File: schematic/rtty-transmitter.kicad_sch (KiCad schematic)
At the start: 67 parts, among them J1 USB_B, J2 USBasp header, J3 Conn_Coaxial, J4 Conn_01x02_Pin, J5 Conn_01x02_Pin, J6 Conn_01x02_Pin, Q1 PN2222A, Q2 PN2222A, U1 MCP2221AxP, U2 ATmega328P-P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

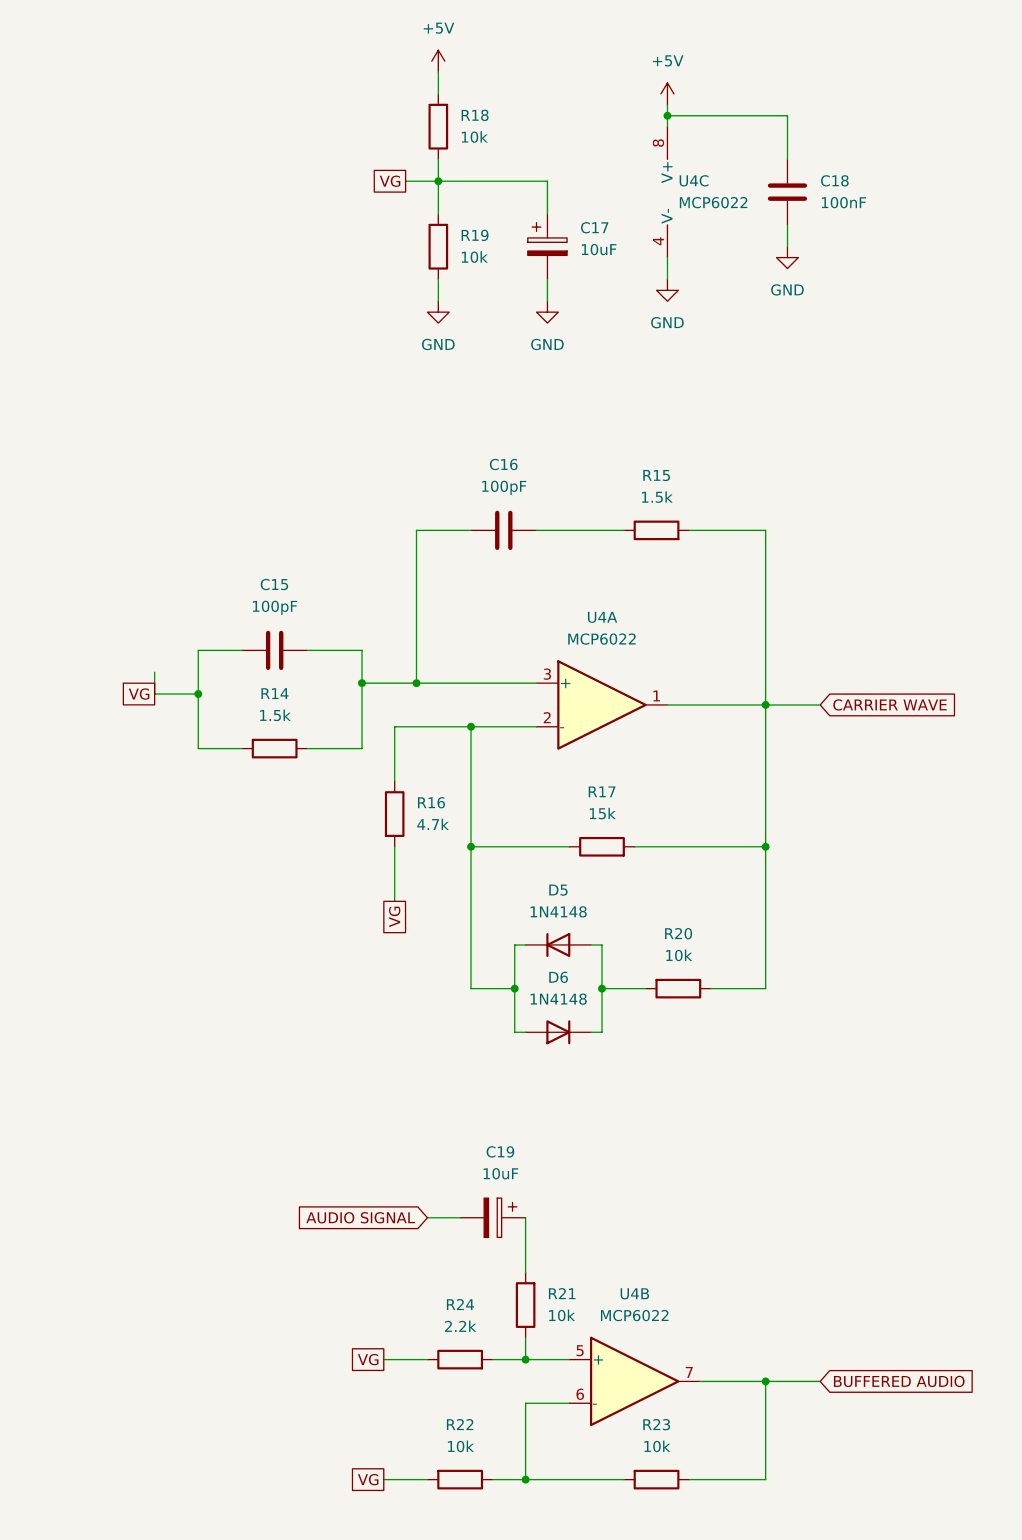
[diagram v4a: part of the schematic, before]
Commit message: Schematic: Test points added
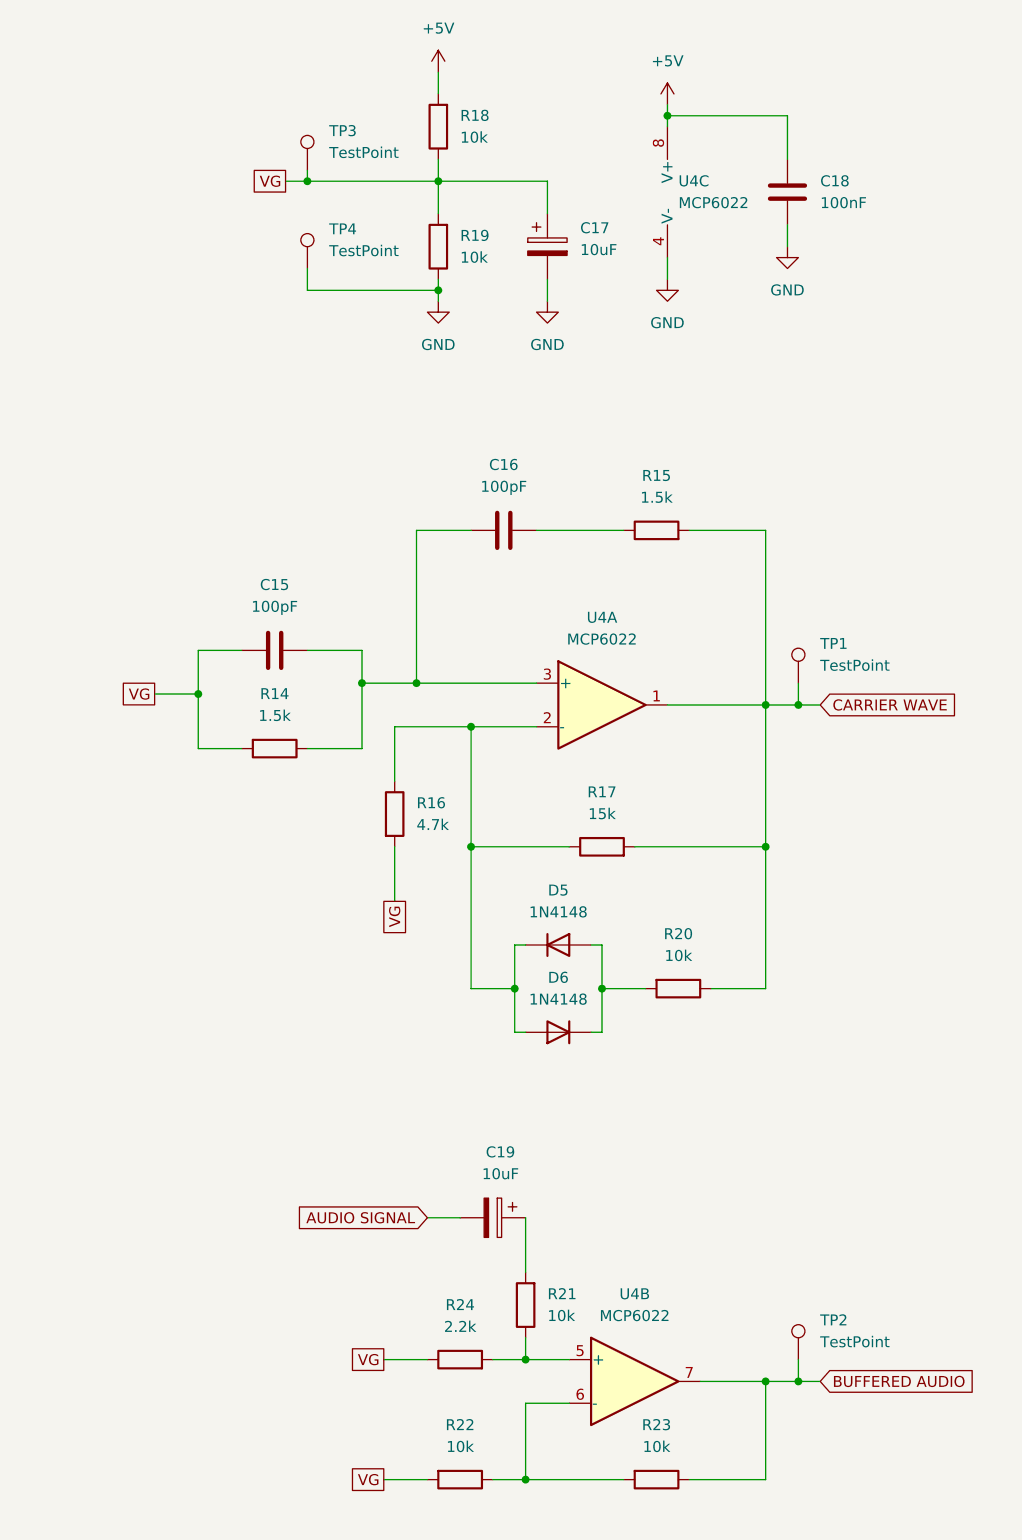
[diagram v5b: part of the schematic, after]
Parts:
- added TP1, TP2, TP3, TP4: TestPoint, TestPoint:TestPoint_Plated_Hole_D2.0mm, symbol Connector:TestPoint
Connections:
- net BUFFERED AUDIO: now also TP2.1
- net CARRIER WAVE: now also TP1.1
- net GND: now also TP4.1
- net VG: now also TP3.1
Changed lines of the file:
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@@
   (junction (at 194.31 124.46) (diameter 0) (color 0 0 0 0)
   )
+  (junction (at 335.28 55.88) (diameter 0) (color 0 0 0 0)
+  )
   (junction (at 180.34 81.28) (diameter 0) (color 0 0 0 0)
   )
   (junction (at 200.66 252.73) (diameter 0) (color 0 0 0 0)
   )
+  (junction (at 377.19 182.88) (diameter 0) (color 0 0 0 0)
+  )
   (junction (at 53.34 185.42) (diameter 0) (color 0 0 0 0)
   )
@@
   (junction (at 248.92 54.61) (diameter 0) (color 0 0 0 0)
   )
+  (junction (at 320.04 43.18) (diameter 0) (color 0 0 0 0)
+  )
   (junction (at 92.71 127) (diameter 0) (color 0 0 0 0)
   )
@@
   (junction (at 339.09 106.68) (diameter 0) (color 0 0 0 0)
   )
+  (junction (at 377.19 104.14) (diameter 0) (color 0 0 0 0)
+  )
   (junction (at 335.28 43.18) (diameter 0) (color 0 0 0 0)
   )
@@
     (stroke (width 0) (type default))
   )
-  (wire (pts (xy 373.38 104.14) (xy 379.73 104.14))
+  (wire (pts (xy 373.38 104.14) (xy 377.19 104.14))
     (stroke (width 0) (type default))
   )
@@
     (stroke (width 0) (type default))
   )
+  (wire (pts (xy 320.04 55.88) (xy 335.28 55.88))
+    (stroke (width 0) (type default))
+  )
   (wire (pts (xy 200.66 241.3) (xy 200.66 243.84))
     (stroke (width 0) (type default))
@@
     (stroke (width 0) (type default))
   )
+  (wire (pts (xy 320.04 53.34) (xy 320.04 55.88))
+    (stroke (width 0) (type default))
+  )
   (wire (pts (xy 246.38 87.63) (xy 226.06 87.63))
     (stroke (width 0) (type default))
@@
     (stroke (width 0) (type default))
   )
+  (wire (pts (xy 377.19 101.6) (xy 377.19 104.14))
+    (stroke (width 0) (type default))
+  )
   (wire (pts (xy 67.31 66.04) (xy 67.31 58.42))
     (stroke (width 0) (type default))
@@
     (stroke (width 0) (type default))
   )
+  (wire (pts (xy 377.19 182.88) (xy 379.73 182.88))
+    (stroke (width 0) (type default))
+  )
   (wire (pts (xy 320.04 109.22) (xy 326.39 109.22))
     (stroke (width 0) (type default))
@@
     (stroke (width 0) (type default))
   )
-  (wire (pts (xy 335.28 54.61) (xy 335.28 57.15))
+  (wire (pts (xy 335.28 54.61) (xy 335.28 55.88))
     (stroke (width 0) (type default))
   )
@@
     (stroke (width 0) (type default))
   )
+  (wire (pts (xy 377.19 104.14) (xy 379.73 104.14))
+    (stroke (width 0) (type default))
+  )
   (wire (pts (xy 367.03 137.16) (xy 373.38 137.16))
     (stroke (width 0) (type default))
@@
     (stroke (width 0) (type default))
   )
+  (wire (pts (xy 335.28 55.88) (xy 335.28 57.15))
+    (stroke (width 0) (type default))
+  )
   (wire (pts (xy 232.41 207.01) (xy 245.11 207.01))
     (stroke (width 0) (type default))
@@
     (stroke (width 0) (type default))
   )
+  (wire (pts (xy 320.04 41.91) (xy 320.04 43.18))
+    (stroke (width 0) (type default))
+  )
   (wire (pts (xy 190.5 121.92) (xy 194.31 121.92))
     (stroke (width 0) (type default))
@@
     (stroke (width 0) (type default))
   )
-  (wire (pts (xy 373.38 182.88) (xy 379.73 182.88))
+  (wire (pts (xy 373.38 182.88) (xy 377.19 182.88))
     (stroke (width 0) (type default))
   )
@@
     (stroke (width 0) (type default))
   )
-  (wire (pts (xy 331.47 43.18) (xy 335.28 43.18))
+  (wire (pts (xy 317.5 43.18) (xy 320.04 43.18))
     (stroke (width 0) (type default))
   )
@@
     (stroke (width 0) (type default))
   )
-  (wire (pts (xy 302.26 102.87) (xy 302.26 100.33))
-    (stroke (width 0) (type default))
-  )
   (wire (pts (xy 95.25 78.74) (xy 95.25 130.81))
     (stroke (width 0) (type default))
@@
     (stroke (width 0) (type default))
   )
+  (wire (pts (xy 320.04 43.18) (xy 335.28 43.18))
+    (stroke (width 0) (type default))
+  )
   (wire (pts (xy 152.4 104.14) (xy 152.4 149.86))
     (stroke (width 0) (type default))
@@
     (stroke (width 0) (type default))
   )
+  (wire (pts (xy 377.19 180.34) (xy 377.19 182.88))
+    (stroke (width 0) (type default))
+  )
   (wire (pts (xy 88.9 115.57) (xy 92.71 115.57))
     (stroke (width 0) (type default))
@@
     )
   )
-  (global_label "VG" (shape passive) (at 331.47 43.18 180) (fields_autoplaced)
+  (global_label "VG" (shape passive) (at 317.5 43.18 180) (fields_autoplaced)
     (effects (font (size 1.27 1.27)) (justify right))
-    (property "Intersheetrefs" "${INTERSHEET_REFS}" (at 327.2375 43.18 0)
+    (property "Intersheetrefs" "${INTERSHEET_REFS}" (at 313.2675 43.18 0)
       (effects (font (size 1.27 1.27)) (justify right) hide)
     )
@@
     )
   )
+  (symbol (lib_id "Connector:TestPoint") (at 320.04 41.91 0) (unit 1)
+    (in_bom yes) (on_board yes) (dnp no) (fields_autoplaced)
+    (property "Reference" "TP3" (at 322.58 37.338 0)
+      (effects (font (size 1.27 1.27)) (justify left))
+    )
+    (property "Value" "TestPoint" (at 322.58 39.878 0)
+      (effects (font (size 1.27 1.27)) (justify left))
+    )
+    (property "Footprint" "TestPoint:TestPoint_Plated_Hole_D2.0mm" (at 325.12 41.91 0)
+      (effects (font (size 1.27 1.27)) hide)
+    )
+    (property "Datasheet" "~" (at 325.12 41.91 0)
+      (effects (font (size 1.27 1.27)) hide)
+    )
+    (pin "1")
+    (instances
+      (project "rtty-transmitter"
+        (path "/4ea8d87c-4bb0-4c80-84f6-8dbfd2cdcfd6"
+          (reference "TP3") (unit 1)
+        )
+      )
+    )
+  )
+  (symbol (lib_id "Connector:TestPoint") (at 377.19 180.34 0) (unit 1)
+    (in_bom yes) (on_board yes) (dnp no) (fields_autoplaced)
+    (property "Reference" "TP2" (at 379.73 175.768 0)
+      (effects (font (size 1.27 1.27)) (justify left))
+    )
+    (property "Value" "TestPoint" (at 379.73 178.308 0)
+      (effects (font (size 1.27 1.27)) (justify left))
+    )
+    (property "Footprint" "TestPoint:TestPoint_Plated_Hole_D2.0mm" (at 382.27 180.34 0)
+      (effects (font (size 1.27 1.27)) hide)
+    )
+    (property "Datasheet" "~" (at 382.27 180.34 0)
+      (effects (font (size 1.27 1.27)) hide)
+    )
+    (pin "1")
+    (instances
+      (project "rtty-transmitter"
+        (path "/4ea8d87c-4bb0-4c80-84f6-8dbfd2cdcfd6"
+          (reference "TP2") (unit 1)
+        )
+      )
+    )
+  )
   (symbol (lib_id "StockLib:R_10k") (at 330.2 116.84 0) (unit 1)
     (in_bom yes) (on_board yes) (dnp no) (fields_autoplaced)
@@
     )
   )
+  (symbol (lib_id "Connector:TestPoint") (at 320.04 53.34 0) (unit 1)
+    (in_bom yes) (on_board yes) (dnp no) (fields_autoplaced)
+    (property "Reference" "TP4" (at 322.58 48.768 0)
+      (effects (font (size 1.27 1.27)) (justify left))
+    )
+    (property "Value" "TestPoint" (at 322.58 51.308 0)
+      (effects (font (size 1.27 1.27)) (justify left))
+    )
+    (property "Footprint" "TestPoint:TestPoint_Plated_Hole_D2.0mm" (at 325.12 53.34 0)
+      (effects (font (size 1.27 1.27)) hide)
+    )
+    (property "Datasheet" "~" (at 325.12 53.34 0)
+      (effects (font (size 1.27 1.27)) hide)
+    )
+    (pin "1")
+    (instances
+      (project "rtty-transmitter"
+        (path "/4ea8d87c-4bb0-4c80-84f6-8dbfd2cdcfd6"
+          (reference "TP4") (unit 1)
+        )
+      )
+    )
+  )
   (symbol (lib_id "power:+5V") (at 40.64 67.31 0) (unit 1)
     (in_bom yes) (on_board yes) (dnp no) (fields_autoplaced)
@@
         )
       )
+    )
+  )
+  (symbol (lib_id "Connector:TestPoint") (at 377.19 101.6 0) (unit 1)
+    (in_bom yes) (on_board yes) (dnp no) (fields_autoplaced)
+    (property "Reference" "TP1" (at 379.73 97.028 0)
+      (effects (font (size 1.27 1.27)) (justify left))
+    )
+    (property "Value" "TestPoint" (at 379.73 99.568 0)
+      (effects (font (size 1.27 1.27)) (justify left))
+    )
+    (property "Footprint" "TestPoint:TestPoint_Plated_Hole_D2.0mm" (at 382.27 101.6 0)
+      (effects (font (size 1.27 1.27)) hide)
+    )
+    (property "Datasheet" "~" (at 382.27 101.6 0)
+      (effects (font (size 1.27 1.27)) hide)
+    )
+    (pin "1")
+    (instances
+      (project "rtty-transmitter"
+        (path "/4ea8d87c-4bb0-4c80-84f6-8dbfd2cdcfd6"
+          (reference "TP1") (unit 1)
+        )
+      )

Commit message: Schematic: Groups added
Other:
- note added: "AM modulator and signal mixer - Current-modulated cascode amplifier"
- note added: "Audio output (optional, for headphones)"
- note added: "Microcontroller circuit"
- note added: "Op-amp A - Wien bridge oscillator for the carrier wave"
- note added: "Op-amp B - Non-inverting amplifier for audio buffering"
- note added: "Op-amp power section"
- note added: "Power LED"
- note added: "Reset circuit"
- note added: "USBasp programming header"
- moved on the sheet: C11, C12, C13, C14, C15, C16, C17, C18, C19, D3, D5, D6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

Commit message: Schematic: Labels reworked
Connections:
- net VG renamed VIRTUAL GROUND
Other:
- note added: "AM modulator (signal mixer) and transmitter - Current-modulated cascode amplifier"
- note added: "Op-amp power section with virtual ground reference (2.5V)"
- note removed: "AM modulator and signal mixer - Current-modulated cascode amplifier"
- note removed: "Op-amp power section"
- title: (none) -> RTTY/AM radio transmitter card with USB serial input
- moved on the sheet: C15, C16, C17, C18, D3, D5, D6, J2, R14, R15, R16, R17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

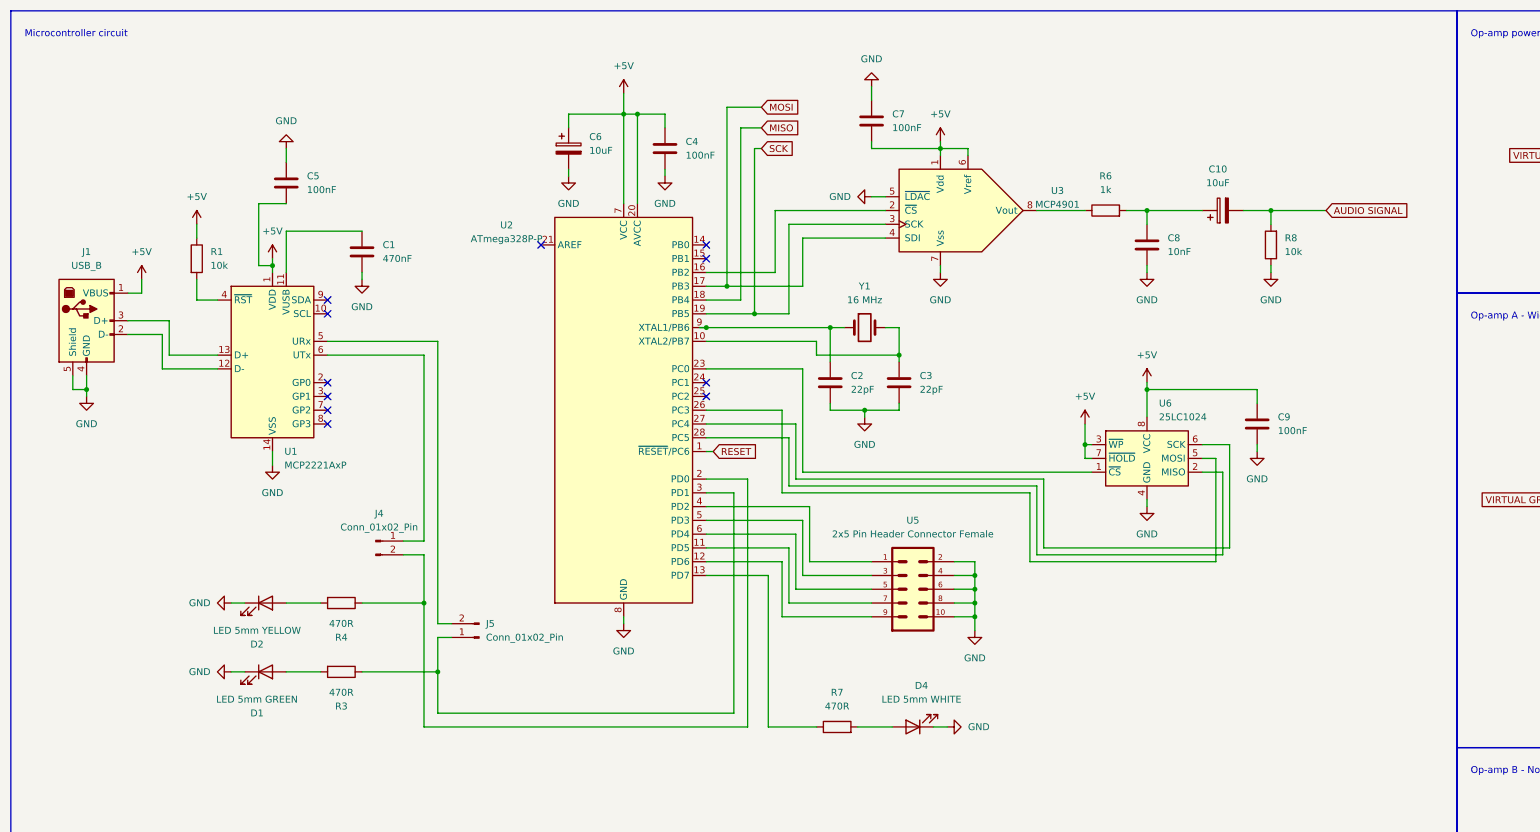
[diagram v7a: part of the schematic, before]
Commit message: Schematic: USB Type B connector symbol updated
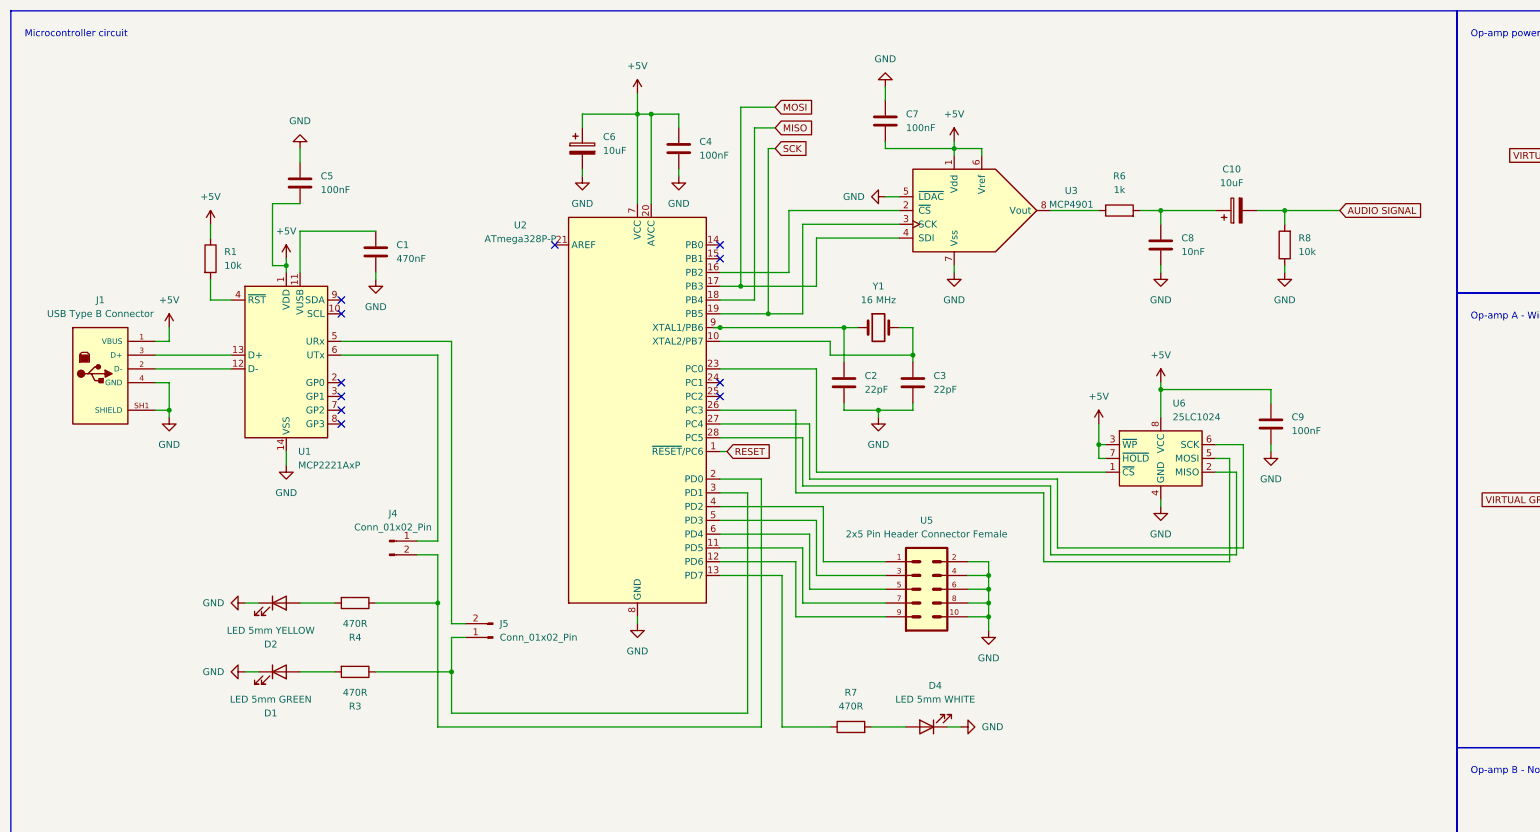
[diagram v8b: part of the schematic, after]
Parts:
- removed J1: USB_B, Connector_USB:USB_B_OST_USB-B1HSxx_Horizontal, symbol Connector:USB_B
- added J1: USB Type B Connector, StockLib:USB Type B Connector, symbol StockLib:USB Type B Connector
- D1: footprint StockLib:LED_D5.0mm_GREEN -> StockLib:LED_D5.0mm_YELLOW
- D4: footprint StockLib:LED_D5.0mm_WHITE -> StockLib:LED_D5.0mm_YELLOW
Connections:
- net +5V: now also J1.1 (VBUS)
- net GND: now also J1.4 (GND), J1.SH1 (SHIELD)
- net at U1.12 (D-): now also J1.2 (D-)
- net at U1.13 (D+): now also J1.3 (D+)
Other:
- moved on the sheet: C1, C10, C2, C3, C4, C5, C6, C7, C8, C9, D1, D2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
